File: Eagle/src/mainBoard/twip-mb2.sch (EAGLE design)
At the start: 17 parts, among them U1 GY-521MPU6050

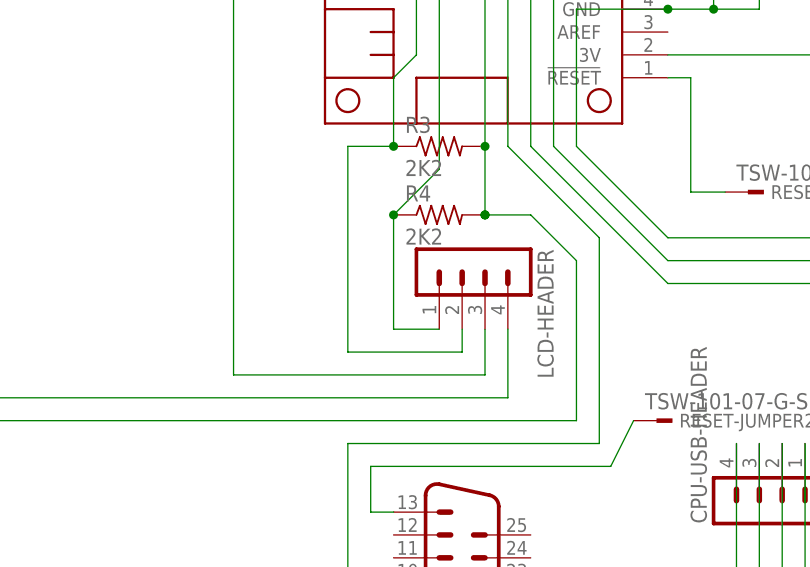
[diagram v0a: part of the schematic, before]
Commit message: Update twip-mb2.sch
uncross I2C leads for LCD cable/header
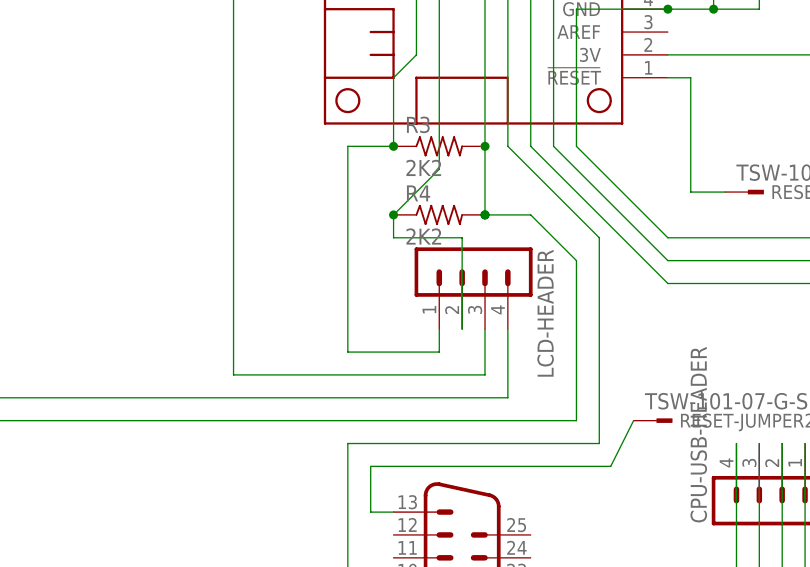
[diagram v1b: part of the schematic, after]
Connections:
- net N$11: now also LCD-HEADER.1; no longer LCD-HEADER.2
- net N$19: now also LCD-HEADER.2; no longer LCD-HEADER.1
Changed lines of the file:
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@@
 <pinref part="MS2" gate="G$1" pin="GPIOSDA"/>
 <wire x1="111.76" y1="149.86" x2="129.54" y2="149.86" width="0.3048" layer="91"/>
-<pinref part="LCD-HEADER" gate="1" pin="1"/>
 <wire x1="129.54" y1="149.86" x2="129.54" y2="101.6" width="0.3048" layer="91"/>
 <pinref part="R4" gate="G$1" pin="1"/>
+<wire x1="124.46" y1="96.52" x2="129.54" y2="101.6" width="0.3048" layer="91"/>
+<wire x1="124.46" y1="96.52" x2="124.46" y2="93.98" width="0.1524" layer="91"/>
 <junction x="124.46" y="96.52"/>
-<wire x1="124.46" y1="96.52" x2="129.54" y2="101.6" width="0.3048" layer="91"/>
-<wire x1="129.54" y1="83.82" x2="124.46" y2="83.82" width="0.3048" layer="91"/>
-<wire x1="124.46" y1="83.82" x2="124.46" y2="96.52" width="0.3048" layer="91"/>
+<wire x1="124.46" y1="93.98" x2="132.08" y2="93.98" width="0.1524" layer="91"/>
+<pinref part="LCD-HEADER" gate="1" pin="2"/>
+<wire x1="132.08" y1="93.98" x2="132.08" y2="83.82" width="0.1524" layer="91"/>
 </segment>
 </net>
@@
 </segment>
 </net>
-<net name="N$11" class="0">
-<segment>
-<pinref part="LCD-HEADER" gate="1" pin="2"/>
-<wire x1="132.08" y1="83.82" x2="132.08" y2="81.28" width="0.3048" layer="91"/>
-<wire x1="127" y1="147.32" x2="127" y2="114.3" width="0.3048" layer="91"/>
-<pinref part="MS2" gate="G$1" pin="GPIOSCL"/>
-<wire x1="111.76" y1="147.32" x2="127" y2="147.32" width="0.3048" layer="91"/>
-<wire x1="132.08" y1="81.28" x2="119.38" y2="81.28" width="0.3048" layer="91"/>
-<wire x1="127" y1="114.3" x2="124.46" y2="111.76" width="0.3048" layer="91"/>
-<pinref part="R3" gate="G$1" pin="1"/>
-<wire x1="124.46" y1="111.76" x2="124.46" y2="104.14" width="0.3048" layer="91"/>
-<junction x="124.46" y="104.14"/>
-<wire x1="124.46" y1="104.14" x2="119.38" y2="104.14" width="0.3048" layer="91"/>
-<wire x1="119.38" y1="104.14" x2="119.38" y2="81.28" width="0.3048" layer="91"/>
-</segment>
-</net>
 <net name="N$21" class="0">
 <segment>
@@
 </segment>
 </net>
+<net name="N$11" class="0">
+<segment>
+<wire x1="119.38" y1="104.14" x2="119.38" y2="81.28" width="0.3048" layer="91"/>
+<pinref part="R3" gate="G$1" pin="1"/>
+<junction x="124.46" y="104.14"/>
+<wire x1="124.46" y1="104.14" x2="119.38" y2="104.14" width="0.3048" layer="91"/>
+<wire x1="124.46" y1="111.76" x2="124.46" y2="104.14" width="0.3048" layer="91"/>
+<wire x1="127" y1="114.3" x2="124.46" y2="111.76" width="0.3048" layer="91"/>
+<wire x1="127" y1="147.32" x2="127" y2="114.3" width="0.3048" layer="91"/>
+<pinref part="MS2" gate="G$1" pin="GPIOSCL"/>
+<wire x1="111.76" y1="147.32" x2="127" y2="147.32" width="0.3048" layer="91"/>
+<wire x1="119.38" y1="81.28" x2="129.54" y2="81.28" width="0.1524" layer="91"/>
+<pinref part="LCD-HEADER" gate="1" pin="1"/>
+<wire x1="129.54" y1="81.28" x2="129.54" y2="83.82" width="0.1524" layer="91"/>
+</segment>
+</net>

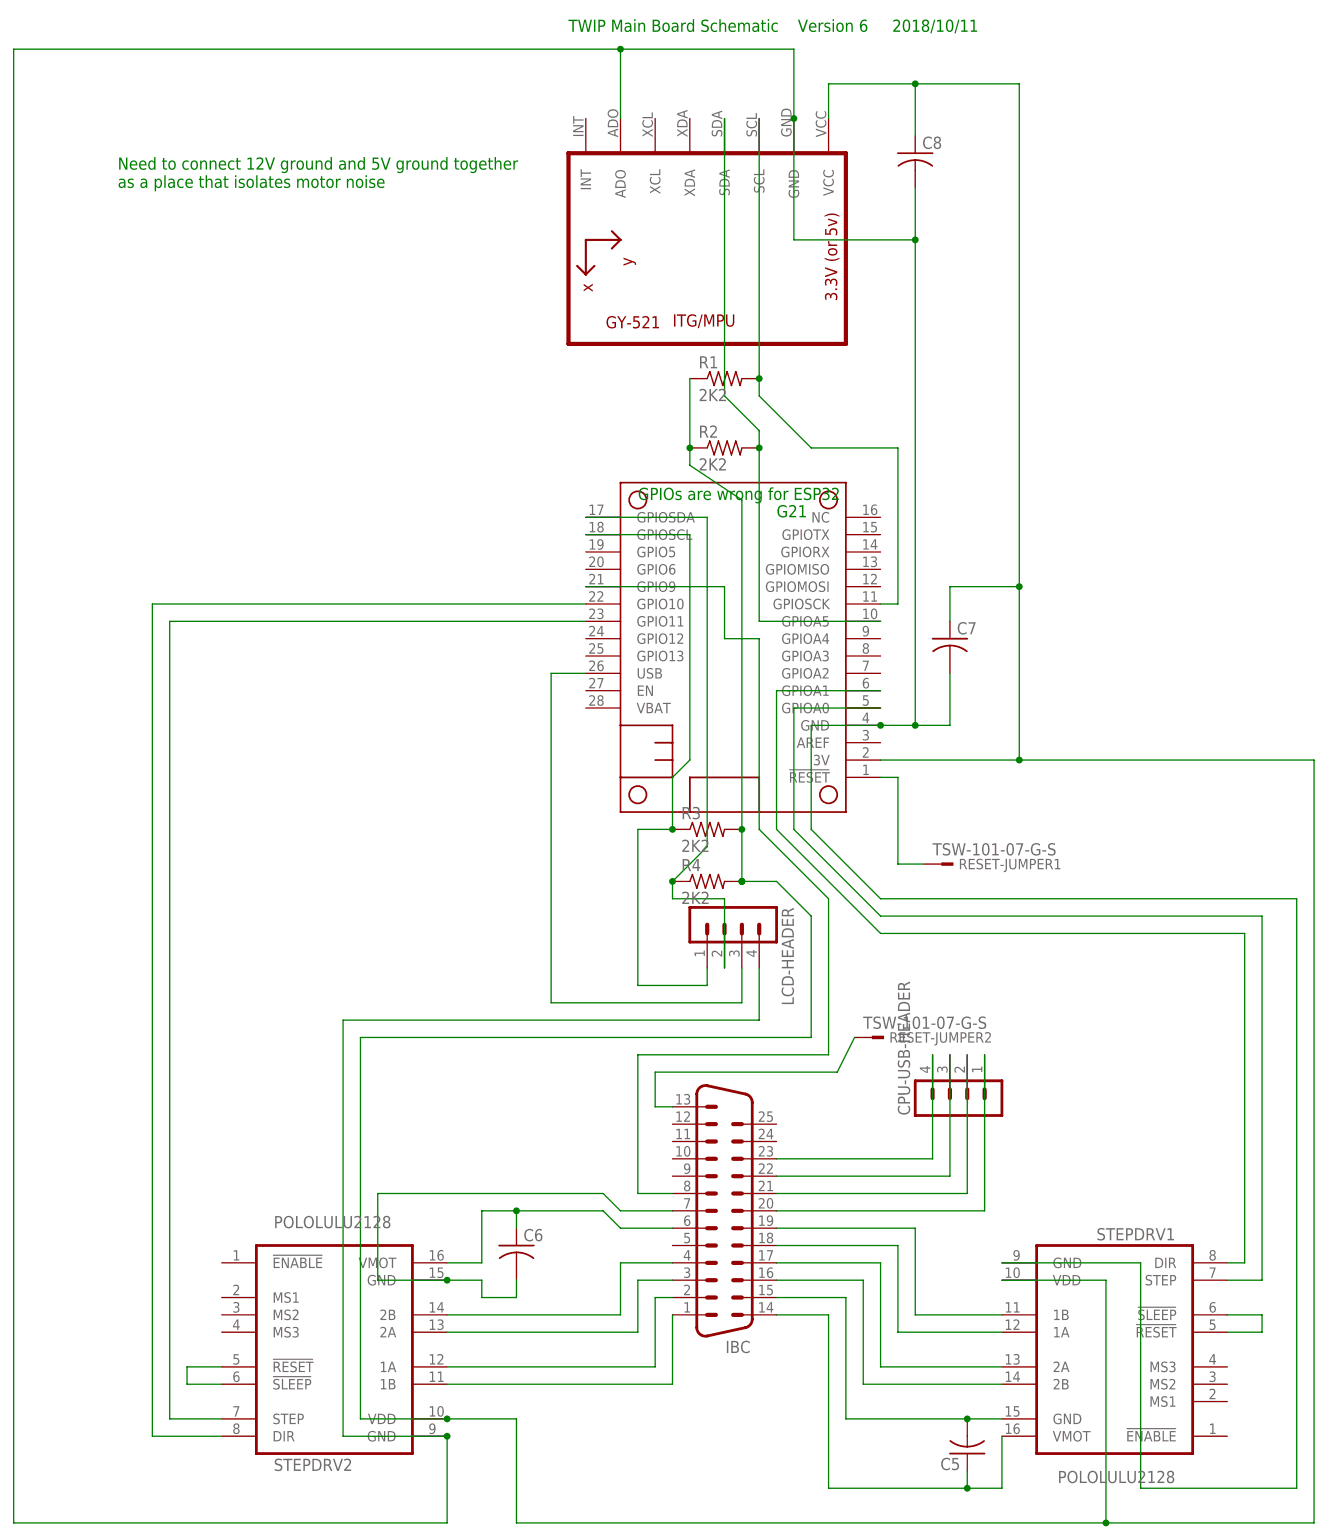
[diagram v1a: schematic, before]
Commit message: Update twip-mb2.sch
major changes - requires PB2
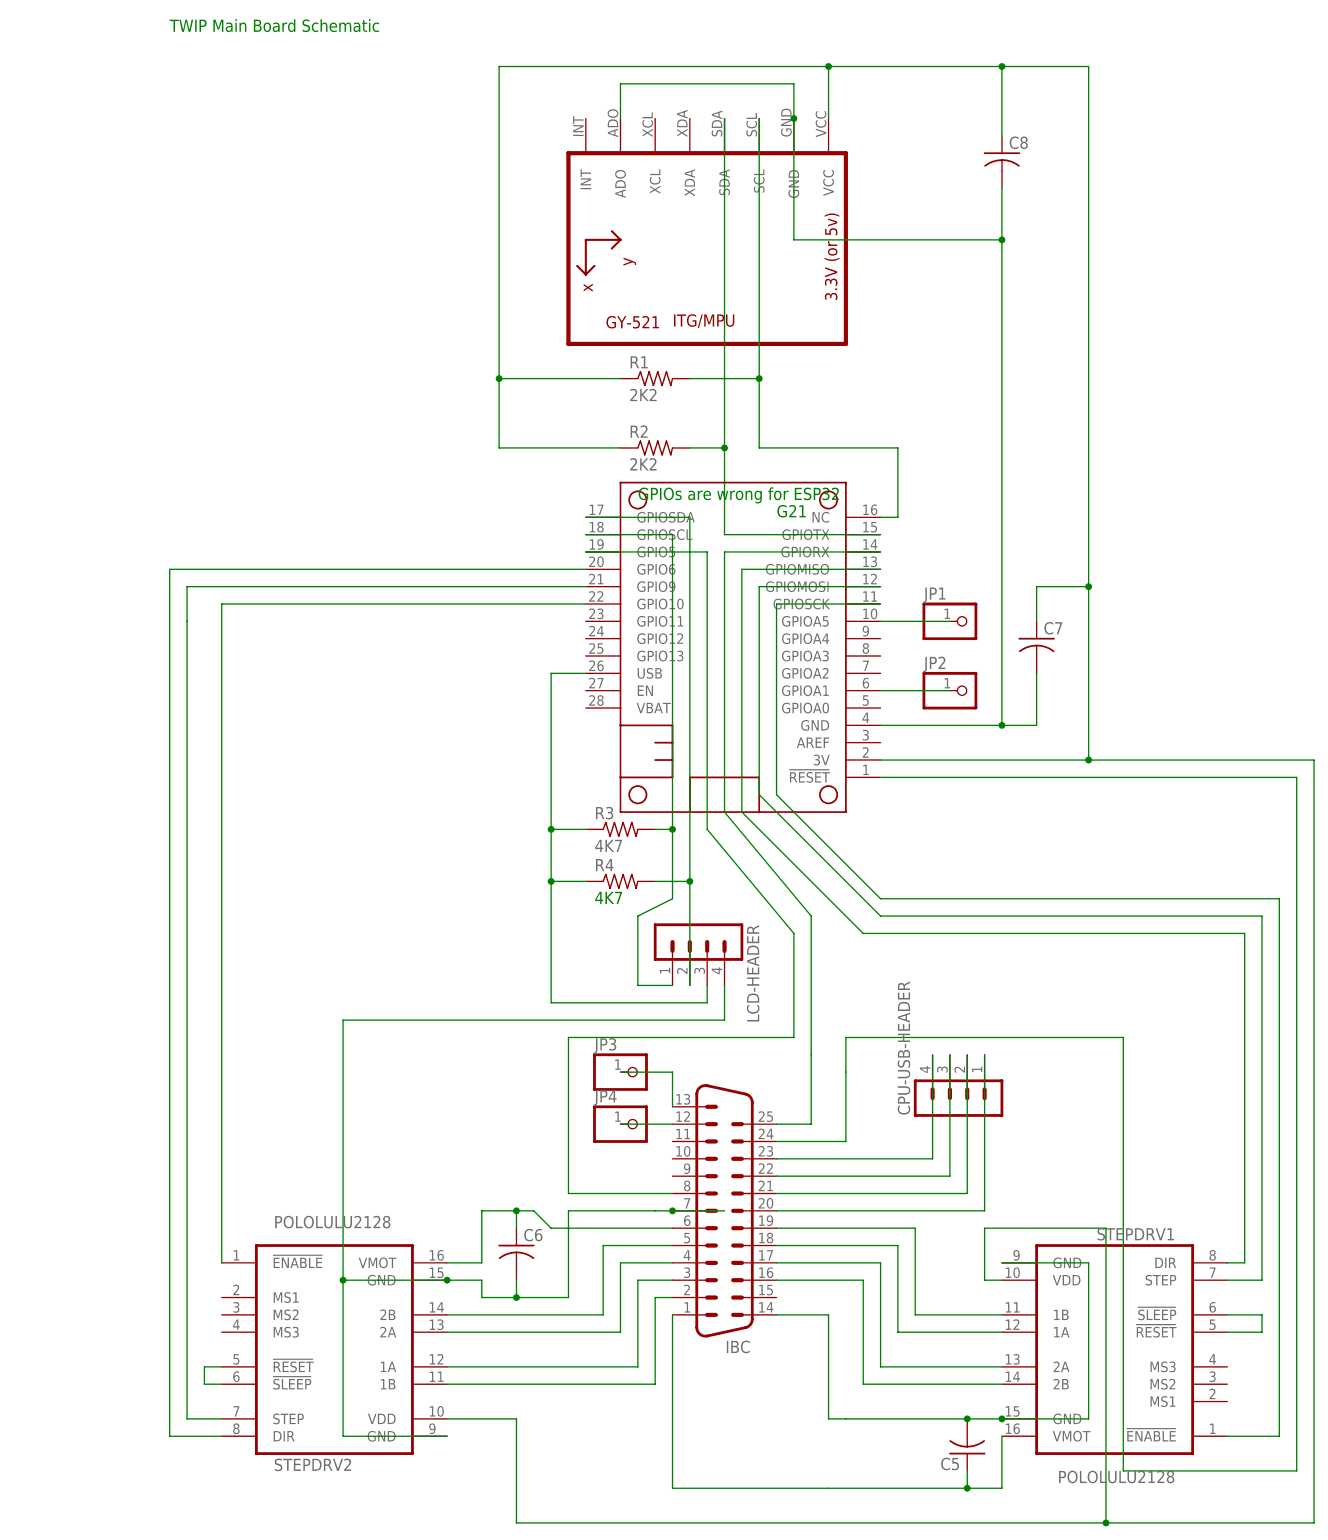
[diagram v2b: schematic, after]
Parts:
- removed RESET-JUMPER1, RESET-JUMPER2: TSW-101-07-G-S, con-samtec:TSW-101-07-G-S
- added JP1, JP2, JP3, JP4: (no value), pinhead:PINHD-1X1
- R3, R4: value 2K2 -> 4K7
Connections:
- removed net N$1: IBCG$1.13, RESET-JUMPER2.1
- new net N$31: JP1.1, MS2.GPIOA5
- new net N$32: MS2.GPIOSCK, STEPDRV1.!ENABLE
- new net N$33: C6.2, IBCG$1.7, LCD-HEADER.4, STEPDRV2.GND@0, STEPDRV2.GND@1
- new net N$34: MS2.GPIO10, STEPDRV2.!ENABLE
- new net N$36: JP2.1, MS2.GPIOA1
- new net N$37: IBCG$1.13, JP3.1
- new net N$38: IBCG$1.12, JP4.1
- net 3V: no longer R3.2, R4.2
- net N$10: now also IBCG$1.4; no longer IBCG$1.3
- net N$11: now also R3.2; no longer R3.1
- net N$12: now also IBCG$1.5; no longer IBCG$1.4
- net N$15: now also MS2.GPIOMISO; no longer MS2.GPIOA1
- net N$16: now also IBCG$1.24; no longer RESET-JUMPER1.1
- net N$17: now also MS2.NC; no longer MS2.GPIOSCK
- net N$19: now also IBCG$1.25, MS2.GPIORX; no longer LCD-HEADER.2, MS2.GPIOSDA, R4.1
- net N$2: now also C7.2, C8.2, MS2.GND, U1.ADO, U1.GND; no longer C6.2, IBCG$1.7, STEPDRV2.GND@0
- net N$20: now also IBCG$1.14, STEPDRV1.GND@1; no longer IBCG$1.15
- net N$22: now also IBCG$1.1; no longer IBCG$1.14
- net N$25: now also MS2.GPIOTX; no longer MS2.GPIOA5
- net N$27: now also MS2.GPIO6; no longer MS2.GPIO10
- net N$28: now also MS2.GPIO5; no longer MS2.GPIO9
- net N$29: now also MS2.GPIO9; no longer MS2.GPIO11
- net N$35: now also LCD-HEADER.2, MS2.GPIOSDA, R4.2; no longer C7.2, C8.2, LCD-HEADER.4, MS2.GND, STEPDRV1.GND@1, STEPDRV2.GND@1, U1.ADO, U1.GND
- net N$5: now also MS2.GPIOMOSI; no longer MS2.GPIOA0
- net N$8: now also IBCG$1.2; no longer IBCG$1.1
- net N$9: now also IBCG$1.3; no longer IBCG$1.2
- net USB: now also R3.1, R4.1
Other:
- note added: "TWIP Main Board Schematic"
- note removed: "Need to connect 12V ground and 5V ground together as a place that isolates motor noise"
- note removed: "TWIP Main Board Schematic Version 6 2018/10/11"
- moved on the sheet: C7, C8, LCD-HEADER, R1, R2, R3, R4

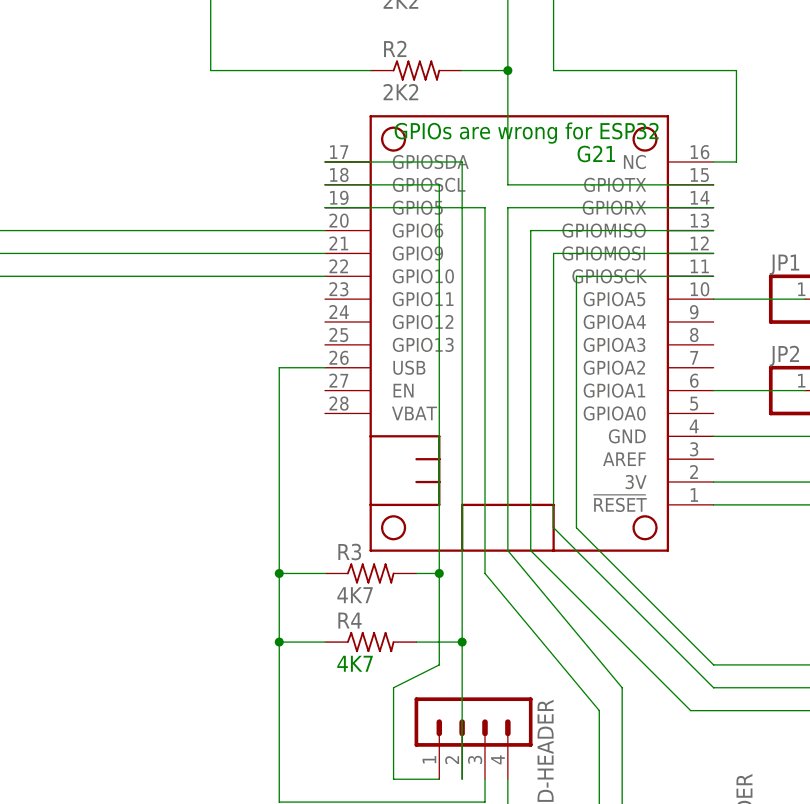
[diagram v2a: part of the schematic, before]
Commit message: Update twip-mb2.sch
a few pin changes, all documented in pinouts doc
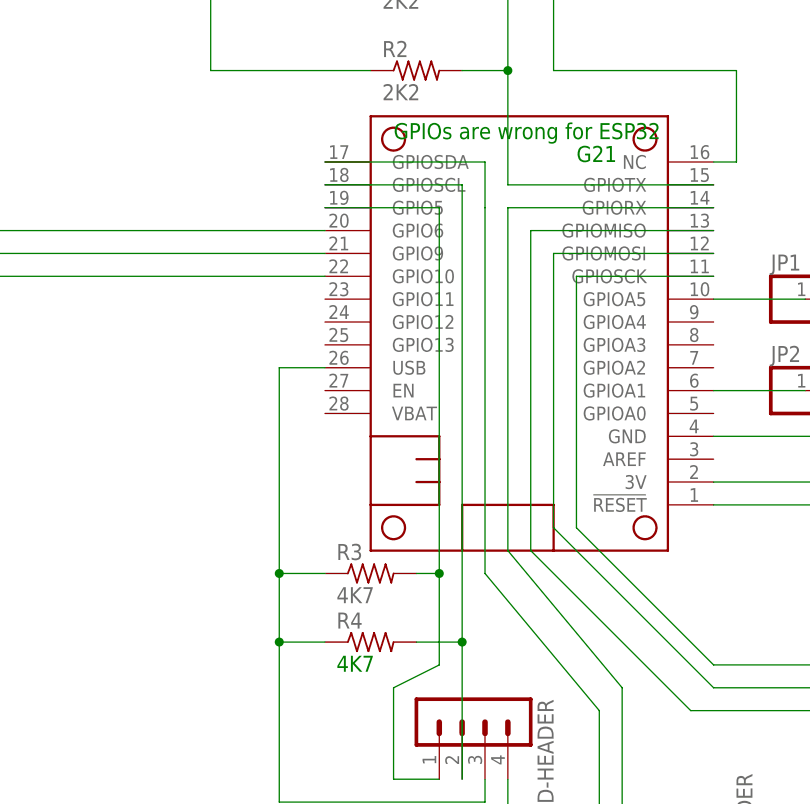
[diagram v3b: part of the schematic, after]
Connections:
- net N$11: now also MS2.GPIO5; no longer MS2.GPIOSCL
- net N$28: now also MS2.GPIOSDA; no longer MS2.GPIO5
- net N$35: now also MS2.GPIOSCL; no longer MS2.GPIOSDA
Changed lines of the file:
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@@
 <wire x1="124.46" y1="50.8" x2="109.22" y2="50.8" width="0.3048" layer="91"/>
 <wire x1="109.22" y1="50.8" x2="109.22" y2="73.66" width="0.3048" layer="91"/>
-<pinref part="MS2" gate="G$1" pin="GPIO5"/>
-<wire x1="129.54" y1="144.78" x2="111.76" y2="144.78" width="0.3048" layer="91"/>
+<pinref part="MS2" gate="G$1" pin="GPIOSDA"/>
+<wire x1="111.76" y1="149.86" x2="129.54" y2="149.86" width="0.1524" layer="91"/>
+<wire x1="129.54" y1="149.86" x2="129.54" y2="144.78" width="0.1524" layer="91"/>
 </segment>
 </net>
@@
 <net name="N$11" class="0">
 <segment>
-<pinref part="MS2" gate="G$1" pin="GPIOSCL"/>
-<wire x1="111.76" y1="147.32" x2="124.46" y2="147.32" width="0.3048" layer="91"/>
 <pinref part="LCD-HEADER" gate="1" pin="1"/>
 <wire x1="119.38" y1="81.28" x2="124.46" y2="81.28" width="0.3048" layer="91"/>
 <wire x1="124.46" y1="93.98" x2="119.38" y2="91.44" width="0.3048" layer="91"/>
 <wire x1="119.38" y1="91.44" x2="119.38" y2="81.28" width="0.3048" layer="91"/>
-<wire x1="124.46" y1="147.32" x2="124.46" y2="104.14" width="0.3048" layer="91"/>
 <pinref part="R3" gate="G$1" pin="2"/>
+<wire x1="124.46" y1="144.78" x2="124.46" y2="104.14" width="0.3048" layer="91"/>
 <wire x1="124.46" y1="104.14" x2="124.46" y2="93.98" width="0.3048" layer="91"/>
 <wire x1="121.92" y1="104.14" x2="124.46" y2="104.14" width="0.3048" layer="91"/>
 <junction x="124.46" y="104.14"/>
+<pinref part="MS2" gate="G$1" pin="GPIO5"/>
+<wire x1="124.46" y1="144.78" x2="111.76" y2="144.78" width="0.1524" layer="91"/>
 </segment>
 </net>
@@
 <wire x1="121.92" y1="96.52" x2="127" y2="96.52" width="0.3048" layer="91"/>
 <wire x1="127" y1="96.52" x2="127" y2="81.28" width="0.3048" layer="91"/>
-<pinref part="MS2" gate="G$1" pin="GPIOSDA"/>
-<wire x1="111.76" y1="149.86" x2="127" y2="149.86" width="0.3048" layer="91"/>
-<wire x1="127" y1="96.52" x2="127" y2="149.86" width="0.3048" layer="91"/>
+<wire x1="127" y1="96.52" x2="127" y2="147.32" width="0.3048" layer="91"/>
 <junction x="127" y="96.52"/>
+<pinref part="MS2" gate="G$1" pin="GPIOSCL"/>
+<wire x1="111.76" y1="147.32" x2="127" y2="147.32" width="0.1524" layer="91"/>
 </segment>
 </net>
